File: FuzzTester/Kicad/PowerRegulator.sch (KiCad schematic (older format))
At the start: 10 parts, among them J5 TestPower_PinHeader, J6 9V Power JST XH, U1 AMS1117-5.0, U2 AMS1117-3.3

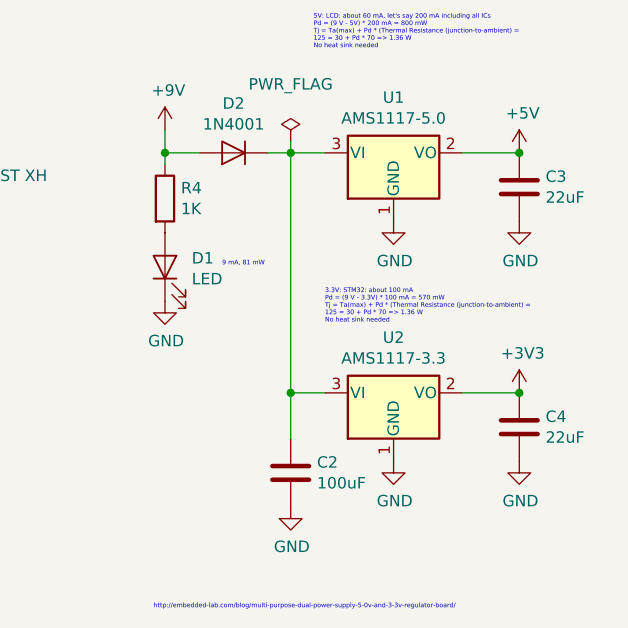
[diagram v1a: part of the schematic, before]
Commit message: Changed power supply
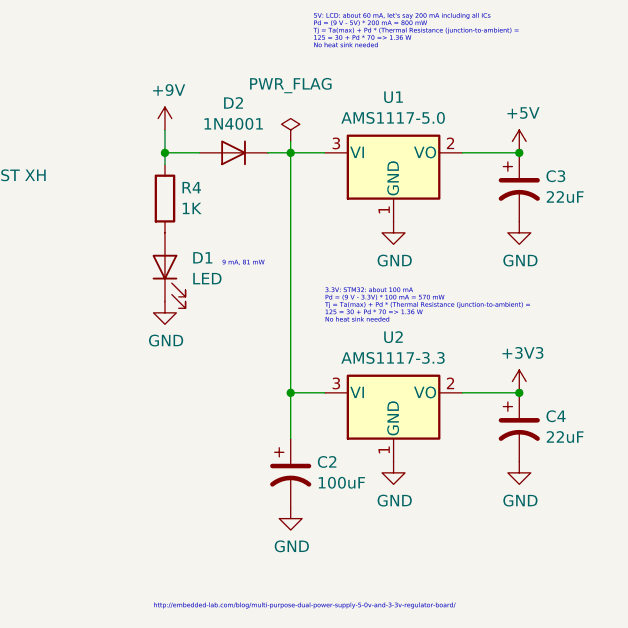
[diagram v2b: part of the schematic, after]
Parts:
- removed C2: 100uF, Capacitor_SMD:C_0805_2012Metric_Pad1.15x1.40mm_HandSolder, symbol Device:C
- removed C3, C4: 22uF, Capacitor_SMD:C_0805_2012Metric_Pad1.15x1.40mm_HandSolder, symbol Device:C
- added C2: 100uF, Capacitor_THT:CP_Radial_D5.0mm_P2.50mm, symbol Device:CP1
- added C3, C4: 22uF, Capacitor_THT:CP_Radial_D5.0mm_P2.50mm, symbol Device:CP1
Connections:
- net +3V3: now also C4.1
- net +5V: now also C3.1
- net GND: now also C2.2, C3.2, C4.2
- net at D2.1 (K), U1.3 (VI), U2.3 (VI): now also C2.1
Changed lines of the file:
@@
-$EndComp
-$Comp
-L Device:C C?
-U 1 1 5E8DF998
-P 4550 1950
-AR Path="/5E8DF998" Ref="C?"  Part="1"
-AR Path="/5E8D81C7/5E8DF998" Ref="C3"  Part="1"
-F 0 "C3" H 4665 1996 50  0000 L CNN
-F 1 "22uF" H 4665 1905 50  0000 L CNN
-F 2 "Capacitor_SMD:C_0805_2012Metric_Pad1.15x1.40mm_HandSolder" H 4588 1800 50  0001 C CNN
-F 3 "~" H 4550 1950 50  0001 C CNN
-	1    4550 1950
-	1    0    0    -1
-$EndComp
-$Comp
-L Device:C C?
-U 1 1 5E8DF99E
-P 4550 3000
-AR Path="/5E8DF99E" Ref="C?"  Part="1"
-AR Path="/5E8D81C7/5E8DF99E" Ref="C4"  Part="1"
-F 0 "C4" H 4665 3046 50  0000 L CNN
-F 1 "22uF" H 4665 2955 50  0000 L CNN
-F 2 "Capacitor_SMD:C_0805_2012Metric_Pad1.15x1.40mm_HandSolder" H 4588 2850 50  0001 C CNN
-F 3 "~" H 4550 3000 50  0001 C CNN
-	1    4550 3000
-	1    0    0    -1
 $EndComp
 $Comp
@@
 	3550 3050 3550 2850
 Connection ~ 3550 2850
-$Comp
-L Device:C C?
-U 1 1 5E8DF9D5
-P 3550 3200
-AR Path="/5E8DF9D5" Ref="C?"  Part="1"
-AR Path="/5E8D81C7/5E8DF9D5" Ref="C2"  Part="1"
-F 0 "C2" H 3665 3246 50  0000 L CNN
-F 1 "100uF" H 3665 3155 50  0000 L CNN
-F 2 "Capacitor_SMD:C_0805_2012Metric_Pad1.15x1.40mm_HandSolder" H 3588 3050 50  0001 C CNN
-F 3 "~" H 3550 3200 50  0001 C CNN
-	1    3550 3200
-	1    0    0    -1
-$EndComp
 $Comp
 L power:+5V #PWR?
@@
 	1    0    0    -1
 $EndComp
-Connection ~ 4550 1800
 Wire Wire Line
 	3450 1800 3550 1800
@@
 	1    0    0    -1
 $EndComp
-Connection ~ 4550 2850
 Wire Wire Line
 	3550 1800 3550 2850
@@
 Wire Wire Line
 	1650 1800 1650 2200
+$Comp
+L Device:CP1 C4
+U 1 1 5E99E117
+P 4550 3000
+F 0 "C4" H 4665 3046 50  0000 L CNN
+F 1 "22uF" H 4665 2955 50  0000 L CNN
+F 2 "Capacitor_THT:CP_Radial_D5.0mm_P2.50mm" H 4550 3000 50  0001 C CNN
+F 3 "~" H 4550 3000 50  0001 C CNN
+	1    4550 3000
+	1    0    0    -1
+$EndComp
+Connection ~ 4550 2850
+$Comp
+L Device:CP1 C3
+U 1 1 5E99F224
+P 4550 1950
+F 0 "C3" H 4665 1996 50  0000 L CNN
+F 1 "22uF" H 4665 1905 50  0000 L CNN
+F 2 "Capacitor_THT:CP_Radial_D5.0mm_P2.50mm" H 4550 1950 50  0001 C CNN
+F 3 "~" H 4550 1950 50  0001 C CNN
+	1    4550 1950
+	1    0    0    -1
+$EndComp
+Connection ~ 4550 1800
+$Comp
+L Device:CP1 C2
+U 1 1 5E99F989
+P 3550 3200
+F 0 "C2" H 3665 3246 50  0000 L CNN
+F 1 "100uF" H 3665 3155 50  0000 L CNN
+F 2 "Capacitor_THT:CP_Radial_D5.0mm_P2.50mm" H 3550 3200 50  0001 C CNN
+F 3 "~" H 3550 3200 50  0001 C CNN
+	1    3550 3200
+	1    0    0    -1
+$EndComp
 $EndSCHEMATC

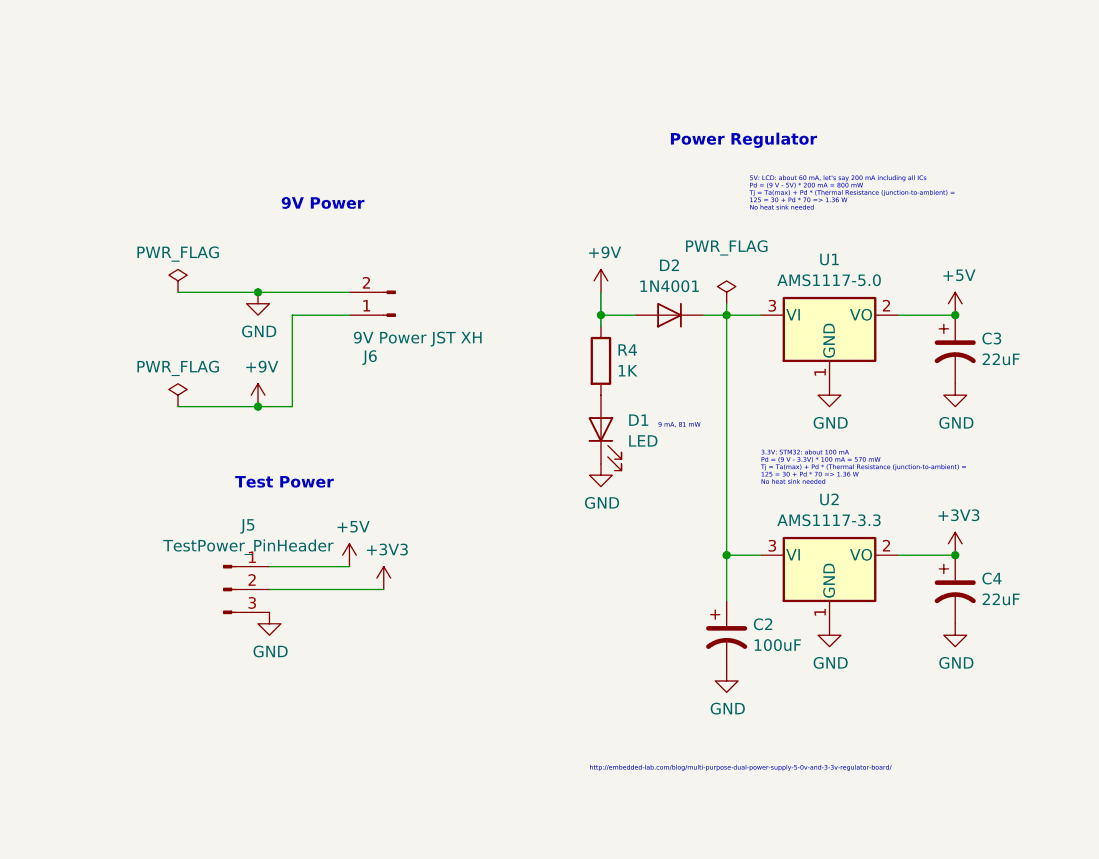
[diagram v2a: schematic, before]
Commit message: Schematics UI/MCU -> MCU + PCB improvements
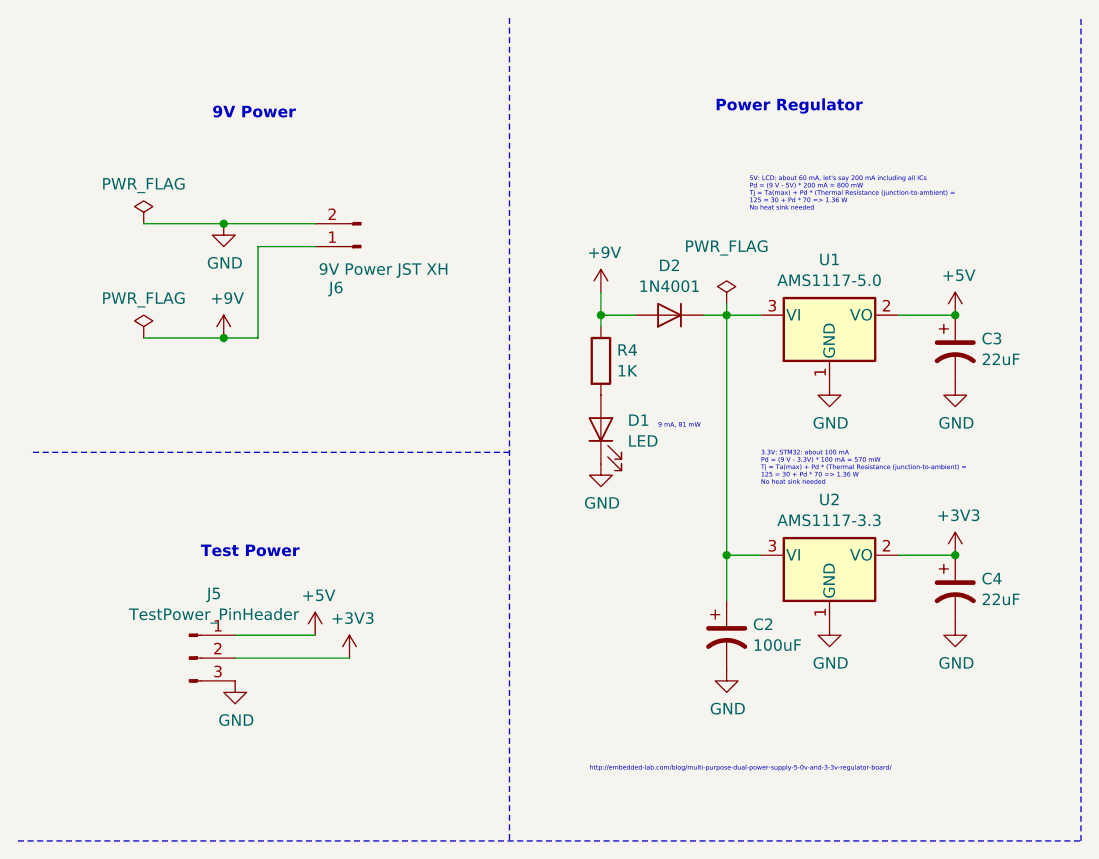
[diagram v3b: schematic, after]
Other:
- moved on the sheet: J5, J6
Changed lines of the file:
@@
 $Descr A4 11693 8268
 encoding utf-8
-Sheet 2 10
+Sheet 2 9
 Title "Guitar Pedal Effect Fuzz Digitally Controlled"
-Date ""
+Date "2020-04-07"
 Rev "0.1"
-Comp ""
+Comp "Michel Keijzers"
 Comment1 ""
-Comment2 ""
-Comment3 ""
-Comment4 ""
+Comment2 "and 2 sets of 8 capacitors (A and D)"
+Comment3 "Guitar pedal effect Fuzz, based on 2 sets of 20 different transistors (B and D)"
+Comment4 "Power Regulator"
 $EndDescr
 $Comp
 L power:+9V #PWR?
 U 1 1 5E8DF95E
-P 1500 2200
+P 1350 1900
 AR Path="/5E8DF95E" Ref="#PWR?"  Part="1"
 AR Path="/5E8D81C7/5E8DF95E" Ref="#PWR06"  Part="1"
-F 0 "#PWR06" H 1500 2050 50  0001 C CNN
-F 1 "+9V" H 1515 2373 50  0000 C CNN
-F 2 "" H 1500 2200 50  0001 C CNN
-F 3 "" H 1500 2200 50  0001 C CNN
-	1    1500 2200
+F 0 "#PWR06" H 1350 1750 50  0001 C CNN
+F 1 "+9V" H 1365 2073 50  0000 C CNN
+F 2 "" H 1350 1900 50  0001 C CNN
+F 3 "" H 1350 1900 50  0001 C CNN
+	1    1350 1900
 	1    0    0    -1
 $EndComp
@@
 L power:PWR_FLAG #FLG?
 U 1 1 5E8DF964
-P 1150 2200
+P 1000 1900
 AR Path="/5E8DF964" Ref="#FLG?"  Part="1"
 AR Path="/5E8D81C7/5E8DF964" Ref="#FLG01"  Part="1"
-F 0 "#FLG01" H 1150 2275 50  0001 C CNN
-F 1 "PWR_FLAG" H 1150 2373 50  0000 C CNN
-F 2 "" H 1150 2200 50  0001 C CNN
-F 3 "~" H 1150 2200 50  0001 C CNN
-	1    1150 2200
-	1    0    0    -1
-$EndComp
-Wire Wire Line
-	1650 2200 1500 2200
-Connection ~ 1500 2200
+F 0 "#FLG01" H 1000 1975 50  0001 C CNN
+F 1 "PWR_FLAG" H 1000 2073 50  0000 C CNN
+F 2 "" H 1000 1900 50  0001 C CNN
+F 3 "~" H 1000 1900 50  0001 C CNN
+	1    1000 1900
+	1    0    0    -1
+$EndComp
+Wire Wire Line
+	1500 1900 1350 1900
+Connection ~ 1350 1900
 $Comp
 L power:GND #PWR?
 U 1 1 5E8DF96C
-P 1500 1700
+P 1350 1400
 AR Path="/5E8DF96C" Ref="#PWR?"  Part="1"
 AR Path="/5E8D81C7/5E8DF96C" Ref="#PWR07"  Part="1"
-F 0 "#PWR07" H 1500 1450 50  0001 C CNN
-F 1 "GND" H 1505 1527 50  0000 C CNN
-F 2 "" H 1500 1700 50  0001 C CNN
-F 3 "" H 1500 1700 50  0001 C CNN
-	1    1500 1700
-	1    0    0    -1
-$EndComp
-Text Notes 1600 1350 0    50   ~ 10
+F 0 "#PWR07" H 1350 1150 50  0001 C CNN
+F 1 "GND" H 1355 1227 50  0000 C CNN
+F 2 "" H 1350 1400 50  0001 C CNN
+F 3 "" H 1350 1400 50  0001 C CNN
+	1    1350 1400
+	1    0    0    -1
+$EndComp
+Text Notes 1300 950  0    50   ~ 10
 9V Power\n
 $Comp
@@
 Wire Wire Line
 	3550 1800 3550 2850
-Text Notes 3300 1150 0    50   ~ 10
+Text Notes 3500 1000 0    50   ~ 10
 Power Regulator\n\n
 Text Notes 2950 3800 0    20   ~ 0
@@
 L Connector:Conn_01x02_Male J?
 U 1 1 5E8DF958
-P 2100 1800
+P 1950 1500
 AR Path="/5E8DF958" Ref="J?"  Part="1"
 AR Path="/5E8D81C7/5E8DF958" Ref="J6"  Part="1"
-F 0 "J6" H 2208 1981 50  0000 C CNN
-F 1 "9V Power JST XH" H 2000 1900 50  0000 C CNN
-F 2 "Connector_JST:JST_XH_B2B-XH-A_1x02_P2.50mm_Vertical" H 2100 1800 50  0001 C CNN
-F 3 "~" H 2100 1800 50  0001 C CNN
-	1    2100 1800
+F 0 "J6" H 2058 1681 50  0000 C CNN
+F 1 "9V Power JST XH" H 1850 1600 50  0000 C CNN
+F 2 "Connector_JST:JST_XH_B2B-XH-A_1x02_P2.50mm_Vertical" H 1950 1500 50  0001 C CNN
+F 3 "~" H 1950 1500 50  0001 C CNN
+	1    1950 1500
 	-1   0    0    1
 $EndComp
 Wire Wire Line
-	1150 2200 1500 2200
+	1000 1900 1350 1900
 $Comp
 L Connector:Conn_01x03_Male J?
 U 1 1 5FACFC6D
-P 1350 3000
+P 1200 3300
 AR Path="/5FACFC6D" Ref="J?"  Part="1"
 AR Path="/5E8D81C7/5FACFC6D" Ref="J5"  Part="1"
-F 0 "J5" H 1458 3281 50  0000 C CNN
-F 1 "TestPower_PinHeader" H 1458 3190 50  0000 C CNN
-F 2 "Connector_PinHeader_2.54mm:PinHeader_1x03_P2.54mm_Vertical" H 1350 3000 50  0001 C CNN
-F 3 "~" H 1350 3000 50  0001 C CNN
-	1    1350 3000
-	1    0    0    -1
-$EndComp
-Text Notes 1400 2650 0    50   ~ 10
+F 0 "J5" H 1308 3581 50  0000 C CNN
+F 1 "TestPower_PinHeader" H 1308 3490 50  0000 C CNN
+F 2 "Connector_PinHeader_2.54mm:PinHeader_1x03_P2.54mm_Vertical" H 1200 3300 50  0001 C CNN
+F 3 "~" H 1200 3300 50  0001 C CNN
+	1    1200 3300
+	1    0    0    -1
+$EndComp
+Text Notes 1250 2950 0    50   ~ 10
 Test Power\n\n
 $Comp
 L power:+5V #PWR0103
 U 1 1 5FACFDD8
-P 1900 2900
-F 0 "#PWR0103" H 1900 2750 50  0001 C CNN
-F 1 "+5V" H 1915 3073 50  0000 C CNN
-F 2 "" H 1900 2900 50  0001 C CNN
-F 3 "" H 1900 2900 50  0001 C CNN
-	1    1900 2900
+P 1750 3200
+F 0 "#PWR0103" H 1750 3050 50  0001 C CNN
+F 1 "+5V" H 1765 3373 50  0000 C CNN
+F 2 "" H 1750 3200 50  0001 C CNN
+F 3 "" H 1750 3200 50  0001 C CNN
+	1    1750 3200
 	1    0    0    -1
 $EndComp
@@
 L power:+3V3 #PWR0104
 U 1 1 5FAD14EB
-P 2050 3000
-F 0 "#PWR0104" H 2050 2850 50  0001 C CNN
-F 1 "+3V3" H 2065 3173 50  0000 C CNN
-F 2 "" H 2050 3000 50  0001 C CNN
-F 3 "" H 2050 3000 50  0001 C CNN
-	1    2050 3000
+P 1900 3300
+F 0 "#PWR0104" H 1900 3150 50  0001 C CNN
+F 1 "+3V3" H 1915 3473 50  0000 C CNN
+F 2 "" H 1900 3300 50  0001 C CNN
+F 3 "" H 1900 3300 50  0001 C CNN
+	1    1900 3300
 	1    0    0    -1
 $EndComp
@@
 L power:GND #PWR?
 U 1 1 5FAD2482
-P 1550 3100
+P 1400 3400
 AR Path="/5FAD2482" Ref="#PWR?"  Part="1"
 AR Path="/5E8D81C7/5FAD2482" Ref="#PWR0105"  Part="1"
-F 0 "#PWR0105" H 1550 2850 50  0001 C CNN
-F 1 "GND" H 1555 2927 50  0000 C CNN
-F 2 "" H 1550 3100 50  0001 C CNN
-F 3 "" H 1550 3100 50  0001 C CNN
-	1    1550 3100
-	1    0    0    -1
-$EndComp
-Wire Wire Line
-	1550 3000 2050 3000
-Wire Wire Line
-	1900 2900 1550 2900
+F 0 "#PWR0105" H 1400 3150 50  0001 C CNN
+F 1 "GND" H 1405 3227 50  0000 C CNN
+F 2 "" H 1400 3400 50  0001 C CNN
+F 3 "" H 1400 3400 50  0001 C CNN
+	1    1400 3400
+	1    0    0    -1
+$EndComp
+Wire Wire Line
+	1400 3300 1900 3300
+Wire Wire Line
+	1750 3200 1400 3200
 $Comp
 L power:PWR_FLAG #FLG?
@@
 L power:PWR_FLAG #FLG?
 U 1 1 5FBDD6C7
-P 1150 1700
+P 1000 1400
 AR Path="/5FBDD6C7" Ref="#FLG?"  Part="1"
 AR Path="/5E8D81C7/5FBDD6C7" Ref="#FLG0105"  Part="1"
-F 0 "#FLG0105" H 1150 1775 50  0001 C CNN
-F 1 "PWR_FLAG" H 1150 1873 50  0000 C CNN
-F 2 "" H 1150 1700 50  0001 C CNN
-F 3 "~" H 1150 1700 50  0001 C CNN
-	1    1150 1700
-	1    0    0    -1
-$EndComp
-Wire Wire Line
-	1150 1700 1500 1700
-Connection ~ 1500 1700
-Wire Wire Line
-	1500 1700 1900 1700
-Wire Wire Line
-	1900 1800 1650 1800
-Wire Wire Line
-	1650 1800 1650 2200
+F 0 "#FLG0105" H 1000 1475 50  0001 C CNN
+F 1 "PWR_FLAG" H 1000 1573 50  0000 C CNN
+F 2 "" H 1000 1400 50  0001 C CNN
+F 3 "~" H 1000 1400 50  0001 C CNN
+	1    1000 1400
+	1    0    0    -1
+$EndComp
+Wire Wire Line
+	1000 1400 1350 1400
+Connection ~ 1350 1400
+Wire Wire Line
+	1350 1400 1750 1400
+Wire Wire Line
+	1750 1500 1500 1500
+Wire Wire Line
+	1500 1500 1500 1900
 $Comp
 L Device:CP1 C4
@@
 	1    0    0    -1
 $EndComp
+Wire Notes Line
+	2600 500  2600 4100
+Wire Notes Line
+	5100 4100 5100 500
+Wire Notes Line
+	450  4100 5100 4100
+Wire Notes Line
+	2600 2400 500  2400
 $EndSCHEMATC
